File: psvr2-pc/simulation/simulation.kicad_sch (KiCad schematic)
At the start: 22 parts, among them Q1 PMOS, Q2 Si2301CDS, Q3 PN2222A, Q4 PMOS, Q5 Si2301CDS, Q6 Si2301CDS, Q7 PN2222A

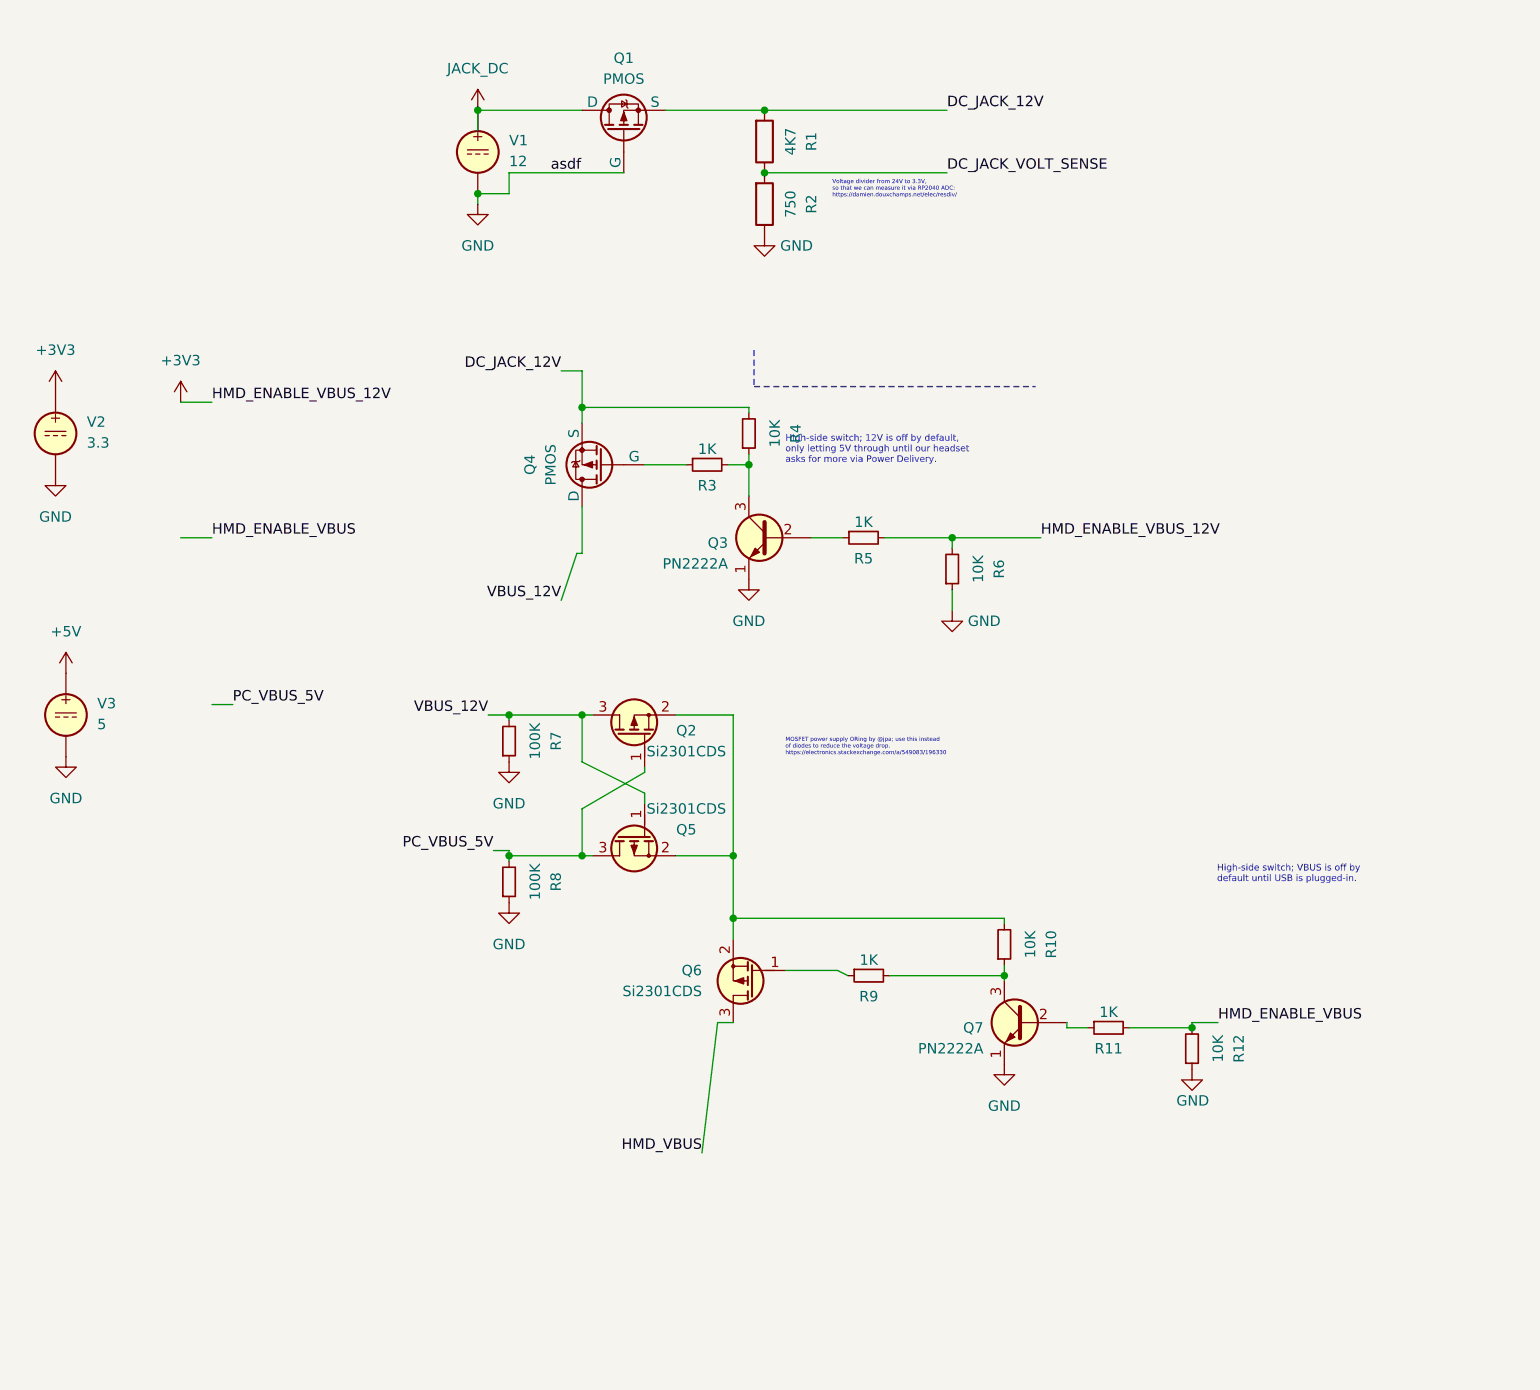
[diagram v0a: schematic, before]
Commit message: Bring more parts of the headset VBUS switch circuit to the simulation. Seems like changing the properties of the existing components isn't enough, I also need to use those symbols.
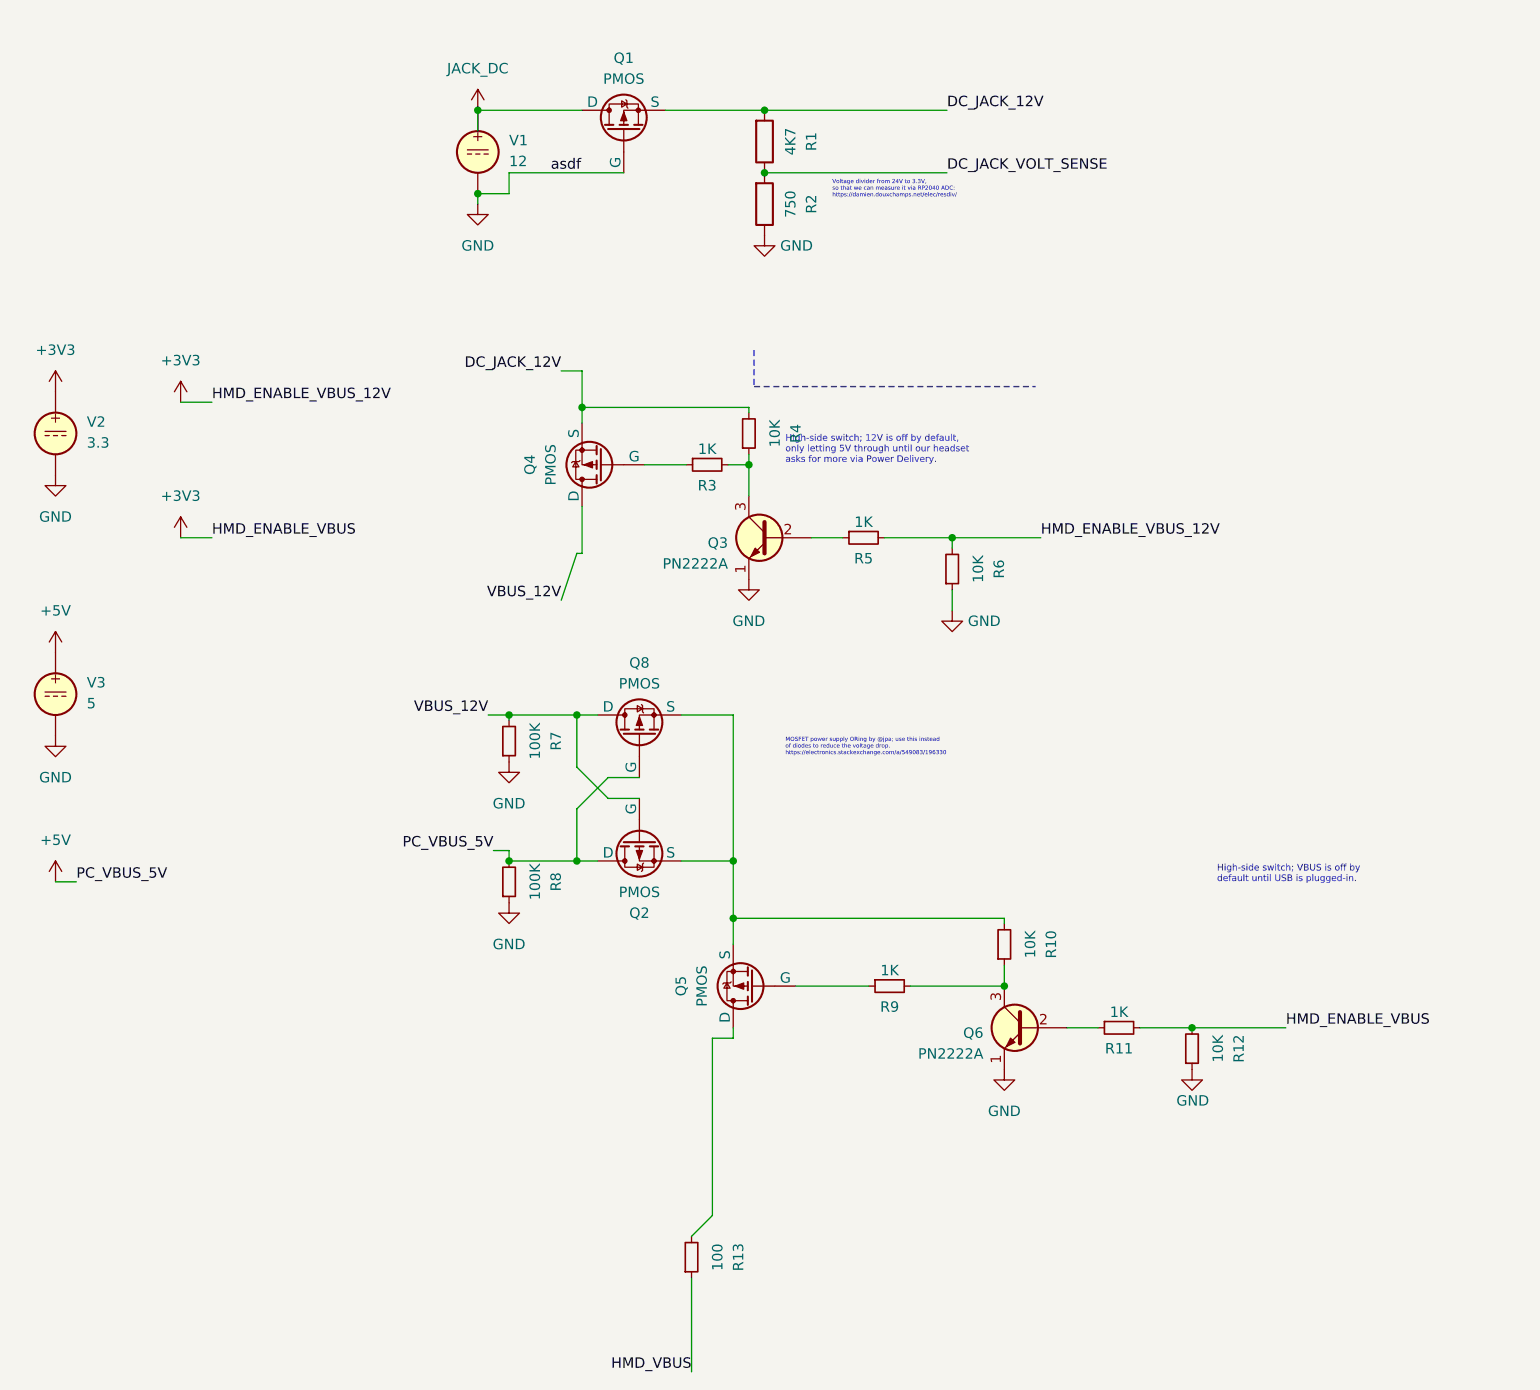
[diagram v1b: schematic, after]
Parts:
- removed Q2, Q5, Q6: Si2301CDS, Package_TO_SOT_SMD:SOT-23, symbol PCM_Transistor_MOSFET_AKL:Si2301CDS
- removed Q7: PN2222A, Package_TO_SOT_SMD:SOT-23, symbol PCM_Transistor_BJT_AKL:PN2222A
- added Q2, Q5, Q8: PMOS, symbol Simulation_SPICE:PMOS
- added Q6: PN2222A, Package_TO_SOT_SMD:SOT-23, symbol PCM_Transistor_BJT_AKL:PN2222A
- added R13: 100, Resistor_SMD:R_0805_2012Metric, symbol Device:R_Small
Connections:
- net HMD_ENABLE_VBUS is gone; now on net +3V3: R11.2, R12.2
- net PC_VBUS_5V is gone; now on net +5V: R8.2
- net +5V: now also Q2.1 (D), Q8.2 (G)
- net GND: now also Q6.1 (E)
- net HMD_VBUS: now also R13.1
- net VBUS_12V: now also Q2.2 (G), Q8.1 (D)
- net at R10.2: now also Q2.3 (S), Q5.3 (S), Q8.3 (S)
- net at R11.1: now also Q6.2 (B)
- net at R10.1, R9.2: now also Q6.3 (C)
- net at R9.1: now also Q5.2 (G)
- new net: Q5.1 (D), R13.2
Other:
- moved on the sheet: R11, R9, V3

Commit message: Hey, look. Got the power circuit simulation to work on KiCad 8 by starting a new project that uses the transistors in the simulation category. Everything seems to more or less work as expected with the default symbols; the reverse voltage protection, the 5V to 12V OR part (you can see the HMD_VBUS orange line staying at 5V and then when the DC jack voltage in green is higher it takes over), and the two programmable power switches (not shown here, they are both enabled in this -24 to +24V voltage sweep). Still learning how all this mumbo jumbo works, but pretty cool.
https://cdn.discordapp.com/attachments/711640844222070836/1216298802143563786/imagen.png?ex=65ffe188&is=65ed6c88&hm=b4e06bf663c617bbf8b1dce227b369c824f3eb81104078d5b9fef80adf1da5ea&

The violet one is the voltage sense line, which remaps the 0-24V range into 0-3.3V so that the microcontroller can read it via ADC and act accordingly; fail safe, and all that.
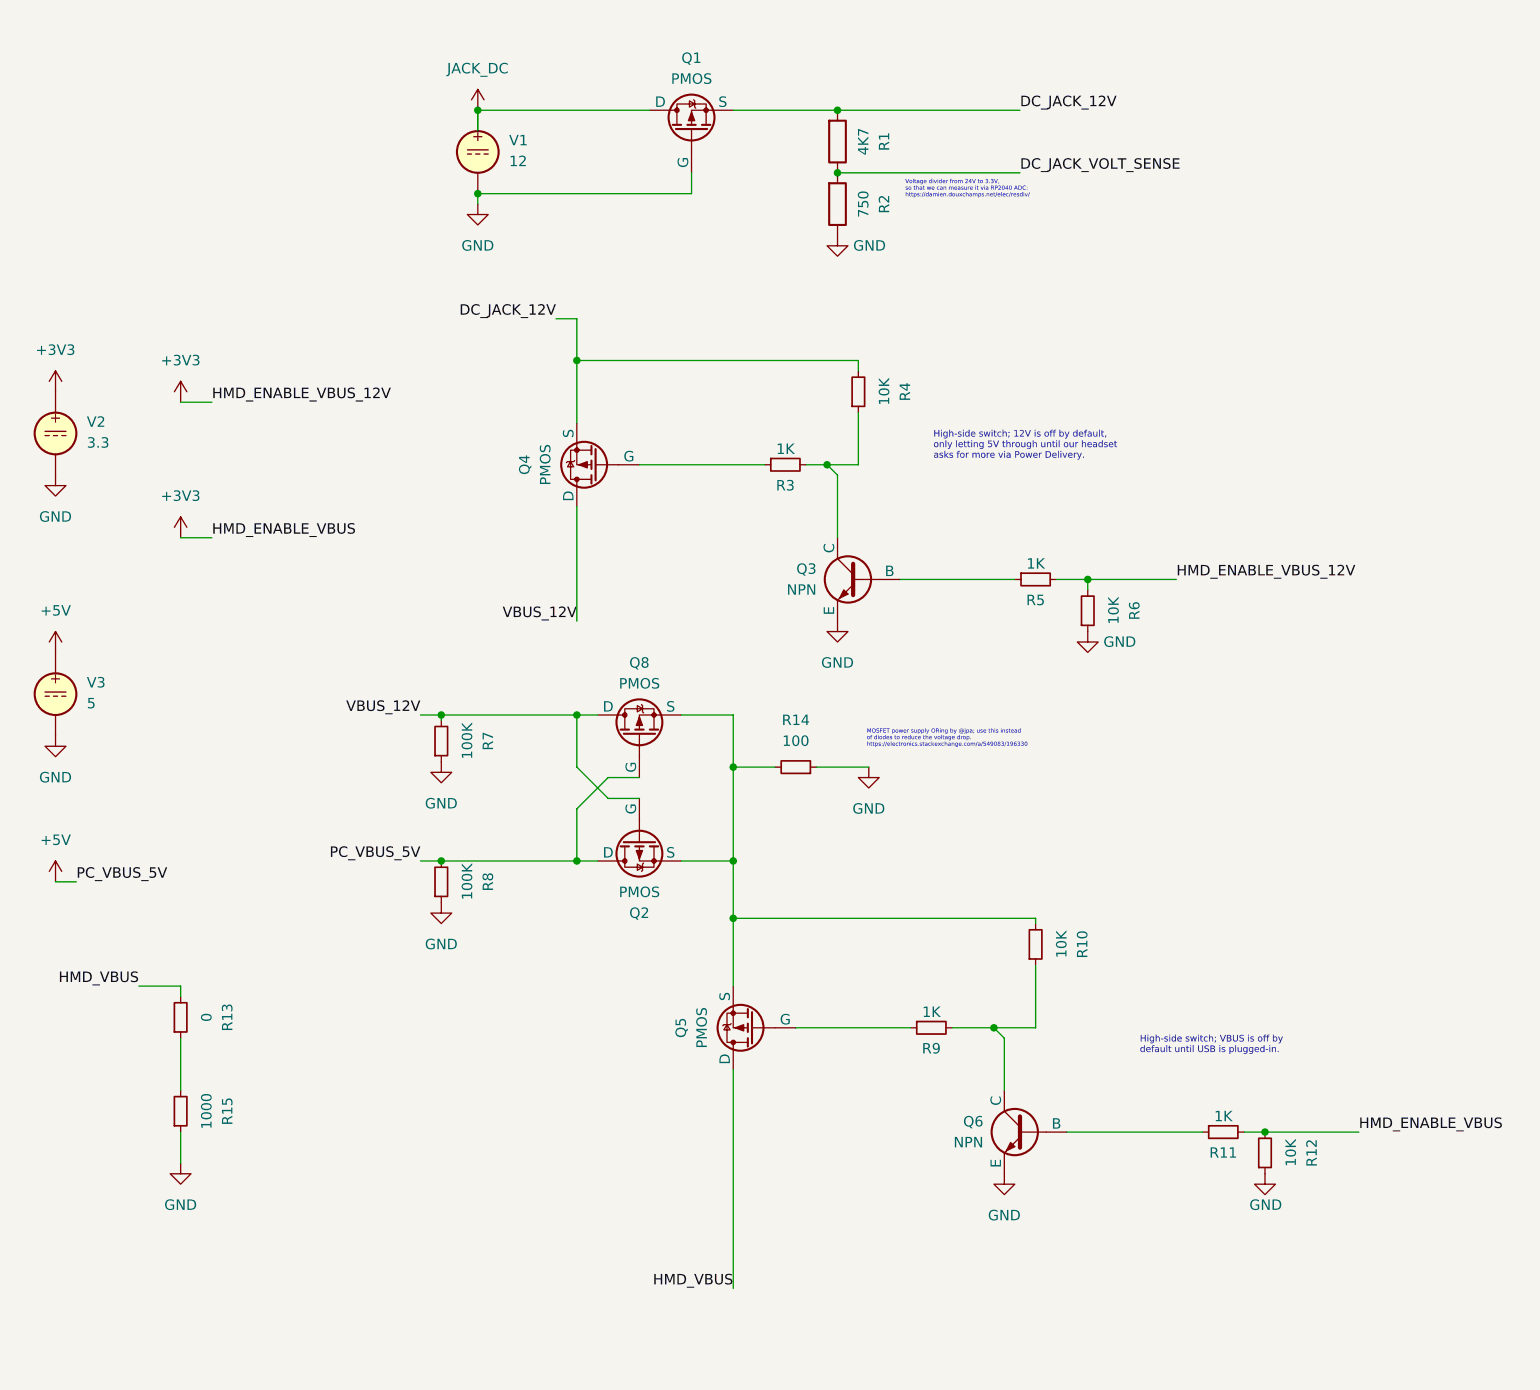
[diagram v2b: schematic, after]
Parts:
- removed Q3, Q6: PN2222A, Package_TO_SOT_SMD:SOT-23, symbol PCM_Transistor_BJT_AKL:PN2222A
- added Q3, Q6: NPN, symbol Simulation_SPICE:NPN
- added R14: 100, Resistor_SMD:R_0805_2012Metric, symbol Device:R_Small
- added R15: 1000, Resistor_SMD:R_0805_2012Metric, symbol Device:R_Small
- R13: value 100 -> 0
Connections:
- net GND: now also Q3.3 (E), Q6.3 (E), R14.1, R15.1
- net HMD_VBUS: now also Q5.1 (D), R13.2; no longer R13.1
- net at R11.1: now also Q6.2 (B)
- net at R10.1, R9.2: now also Q6.1 (C)
- net at Q2.3 (S), Q5.3 (S), Q8.3 (S)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: now also R14.2
- net at R5.1: now also Q3.2 (B)
- net at R3.2, R4.1: now also Q3.1 (C)
- new net: R13.1, R15.2
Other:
- moved on the sheet: Q1, Q4, Q5, R1, R10, R11, R12, R2, R3, R4, R5, R6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
